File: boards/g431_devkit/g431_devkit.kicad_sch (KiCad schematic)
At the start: 0 parts

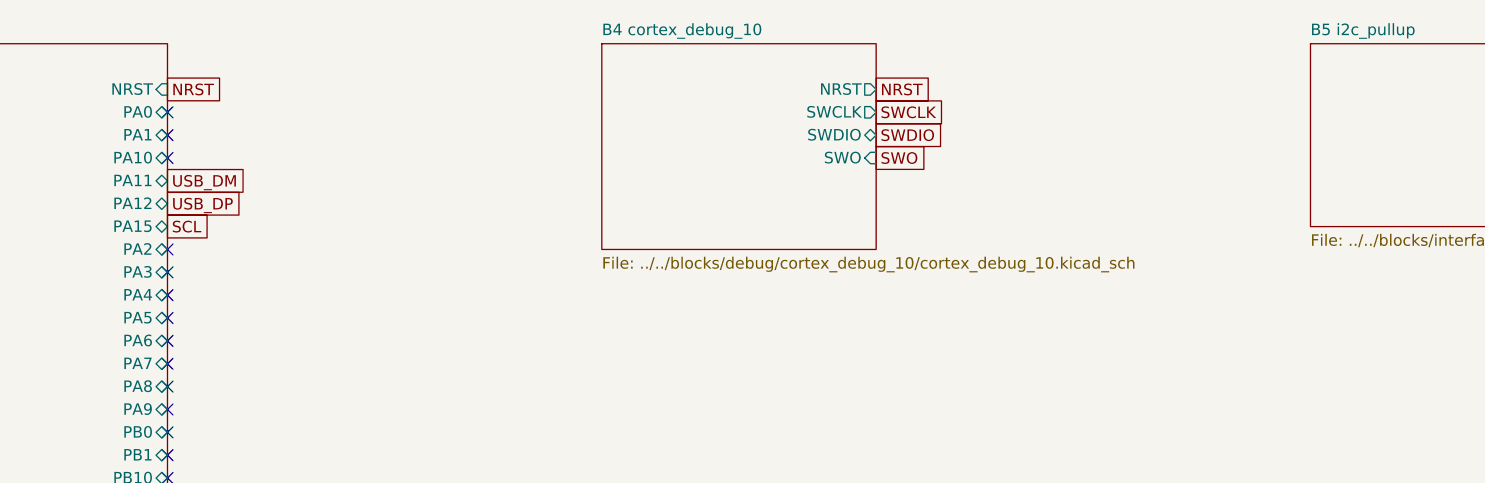
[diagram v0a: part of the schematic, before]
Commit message: g431_devkit 보드: board.json -> 회로도+pins.h+PCB 초기화 (§25 2단계 첫 걸음)
- 완성형 데브킷: stdc14 디버그(UART=USART2 PA2/PA3), USB FS PA11/12,
  I2C1 PB7/PA15. ERC 0/0, 넷 10/10 대조, pins.h 14 defines.
- build_pcb.py (pcbnew): 블록 단위 배치 + 패드-네트 + Edge.Cuts.
  check_board E = pcb drc (미배선만 허용) — DRC 위반 0.
- DRC 실전 적발 수리: LQFP 핀1 실크점 패드 접촉 (pkg_land d1 0.65,
  LQFP48/64 상수 영구화, MCU 2종 재생성 — 원만 이동 diff 2줄) /
  FTSH-107 실크 가로선 패드 관통 (세로 끝선 교체).
- 파일럿 demo_g431_devkit는 완성형으로 대체.

Co-Authored-By: Claude Fable 5 <noreply@anthropic.com>
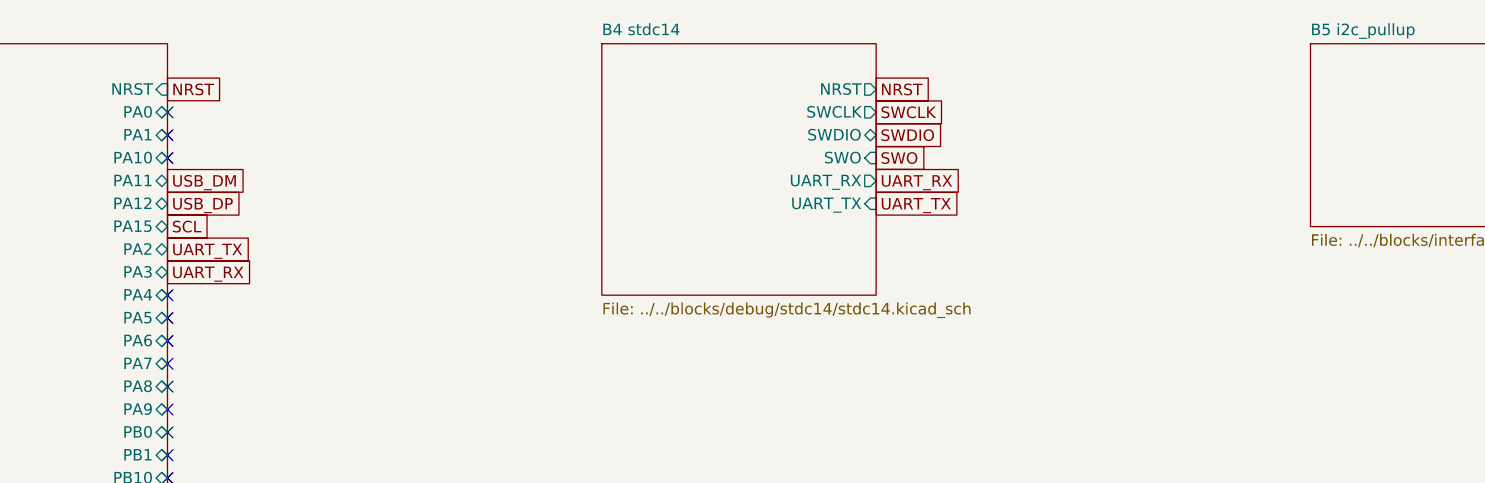
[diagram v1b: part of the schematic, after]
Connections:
- no-connect marks 29 -> 27
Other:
- removed sheet B4 cortex_debug_10
- added sheet B4 stdc14 (../../blocks/debug/stdc14/stdc14.kicad_sch)
- title: STM32G431 devkit demo (USB-C + LDO + SWD + I2C) -> STM32G431 devkit (USB-C + LDO + STDC14 + I2C)
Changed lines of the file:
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@@
 	(paper "A3")
 	(title_block
-		(title "STM32G431 devkit demo (USB-C + LDO + SWD + I2C)")
+		(title "STM32G431 devkit (USB-C + LDO + STDC14 + I2C)")
 		(company "PartReel board")
 		(rev "0.1")
@@
 		)
 	)
+	(global_label "UART_TX"
+		(at 226.06 60.96 0)
+		(effects
+			(font
+				(size 1.27 1.27)
+			)
+			(justify left bottom)
+		)
+	)
+	(global_label "UART_RX"
+		(at 226.06 63.5 0)
+		(effects
+			(font
+				(size 1.27 1.27)
+			)
+			(justify left bottom)
+		)
+	)
 	(global_label "SWO"
 		(at 226.06 104.14 0)
@@
 		)
 	)
+	(global_label "UART_RX"
+		(at 304.8 53.34 0)
+		(effects
+			(font
+				(size 1.27 1.27)
+			)
+			(justify left bottom)
+		)
+	)
+	(global_label "UART_TX"
+		(at 304.8 55.88 0)
+		(effects
+			(font
+				(size 1.27 1.27)
+			)
+			(justify left bottom)
+		)
+	)
 	(global_label "SCL"
 		(at 383.54 43.18 0)
@@
 	(no_connect
 		(at 226.06 50.8)
-	)
-	(no_connect
-		(at 226.06 60.96)
-	)
-	(no_connect
-		(at 226.06 63.5)
 	)
 	(no_connect
@@
 		)
 		(instances
-			(project "demo_g431_devkit"
-				(path "/aac2a15c-b06d-5428-91a2-71073eb09e54"
+			(project "g431_devkit"
+				(path "/e9a219e6-febc-52f2-af91-612ac159a351"
 					(page "2")
 				)
@@
 		)
 		(instances
-			(project "demo_g431_devkit"
-				(path "/aac2a15c-b06d-5428-91a2-71073eb09e54"
+			(project "g431_devkit"
+				(path "/e9a219e6-febc-52f2-af91-612ac159a351"
 					(page "3")
 				)
@@
 		)
 		(instances
-			(project "demo_g431_devkit"
-				(path "/aac2a15c-b06d-5428-91a2-71073eb09e54"
+			(project "g431_devkit"
+				(path "/e9a219e6-febc-52f2-af91-612ac159a351"
 					(page "4")
 				)
@@
 	(sheet
 		(at 274.32 38.1)
-		(size 30.48 22.86)
+		(size 30.48 27.94)
 		(exclude_from_sim no)
 		(in_bom yes)
@@
 			(color 0 0 0 0.0000)
 		)
-		(property "Sheetname" "B4 cortex_debug_10"
+		(property "Sheetname" "B4 stdc14"
 			(at 274.32 37.3 0)
 			(effects
@@
 			)
 		)
-		(property "Sheetfile" "../../blocks/debug/cortex_debug_10/cortex_debug_10.kicad_sch"
-			(at 274.32 61.76 0)
+		(property "Sheetfile" "../../blocks/debug/stdc14/stdc14.kicad_sch"
+			(at 274.32 66.84 0)
 			(effects
 				(font
@@
 			)
 		)
+		(pin "UART_RX" output
+			(at 304.8 53.34 0)
+			(effects
+				(font
+					(size 1.27 1.27)
+				)
+				(justify left)
+			)
+		)
+		(pin "UART_TX" input
+			(at 304.8 55.88 0)
+			(effects
+				(font
+					(size 1.27 1.27)
+				)
+				(justify left)
+			)
+		)
 		(instances
-			(project "demo_g431_devkit"
-				(path "/aac2a15c-b06d-5428-91a2-71073eb09e54"
+			(project "g431_devkit"
+				(path "/e9a219e6-febc-52f2-af91-612ac159a351"
 					(page "5")
 				)
@@
 		)
 		(instances
-			(project "demo_g431_devkit"
-				(path "/aac2a15c-b06d-5428-91a2-71073eb09e54"
+			(project "g431_devkit"
+				(path "/e9a219e6-febc-52f2-af91-612ac159a351"
 					(page "6")
 				)

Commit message: 보드 전역 주석(annotate): 블록 인스턴스별 사본 + 고유 참조번호
- 블록 조합의 참조 중복(U1x2, J1x2 — SMT 작업지시 불가) 해소: build_board가
  블록 sch를 보드 폴더에 인스턴스별 사본으로 넣고 KiCad 계층 주석 방식
  (instances 블록 교체)으로 전역 번호 부여 (U1/U2, J1/J2, C1~C9, R1~R5,
  #PWR/#FLG 포함). R12 자유 텍스트 표기 동기화.
- 보드 폴더 자립형화 (Sheetfile 로컬 — 키캐드/test 복사도 통째로).
- ref_map.json 산출, check_board 넷 대조가 지도 반영. 전 게이트 통과.

Co-Authored-By: Claude Fable 5 <noreply@anthropic.com>
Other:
- sheet B1 usb_c_5v: file ../../blocks/power/usb_c_5v/usb_c_5v.kicad_sch -> B1_usb_c_5v.kicad_sch
- sheet B2 ldo_3v3: file ../../blocks/power/ldo_3v3/ldo_3v3.kicad_sch -> B2_ldo_3v3.kicad_sch
- sheet B3 g431_min: file ../../blocks/mcu/g431_min/g431_min.kicad_sch -> B3_g431_min.kicad_sch
- sheet B4 stdc14: file ../../blocks/debug/stdc14/stdc14.kicad_sch -> B4_stdc14.kicad_sch
- sheet B5 i2c_pullup: file ../../blocks/interface/i2c_pullup/i2c_pullup.kicad_sch -> B5_i2c_pullup.kicad_sch
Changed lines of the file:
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@@
 			)
 		)
-		(property "Sheetfile" "../../blocks/power/usb_c_5v/usb_c_5v.kicad_sch"
+		(property "Sheetfile" "B1_usb_c_5v.kicad_sch"
 			(at 38.1 59.22 0)
 			(effects
@@
 			)
 		)
-		(property "Sheetfile" "../../blocks/power/ldo_3v3/ldo_3v3.kicad_sch"
+		(property "Sheetfile" "B2_ldo_3v3.kicad_sch"
 			(at 116.84 59.22 0)
 			(effects
@@
 			)
 		)
-		(property "Sheetfile" "../../blocks/mcu/g431_min/g431_min.kicad_sch"
+		(property "Sheetfile" "B3_g431_min.kicad_sch"
 			(at 195.58 145.58 0)
 			(effects
@@
 			)
 		)
-		(property "Sheetfile" "../../blocks/debug/stdc14/stdc14.kicad_sch"
+		(property "Sheetfile" "B4_stdc14.kicad_sch"
 			(at 274.32 66.84 0)
 			(effects
@@
 			)
 		)
-		(property "Sheetfile" "../../blocks/interface/i2c_pullup/i2c_pullup.kicad_sch"
+		(property "Sheetfile" "B5_i2c_pullup.kicad_sch"
 			(at 353.06 59.22 0)
 			(effects
